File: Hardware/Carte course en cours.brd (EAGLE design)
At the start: 47 x 28.6 mm, 41 parts, among them J2 AVR_SPI_PROG_3X2NS, J3 PWR IN, J4 RC receiver, J5 ESC, J6 ESC, J7 MICRO-SD_CARD_SOCKET, J8 ESC, U1 V_REG_317SMD, U2 ATMEGA328P_TQFP, U3 FT232RL, U4 MPU6050, Y1 16MHz

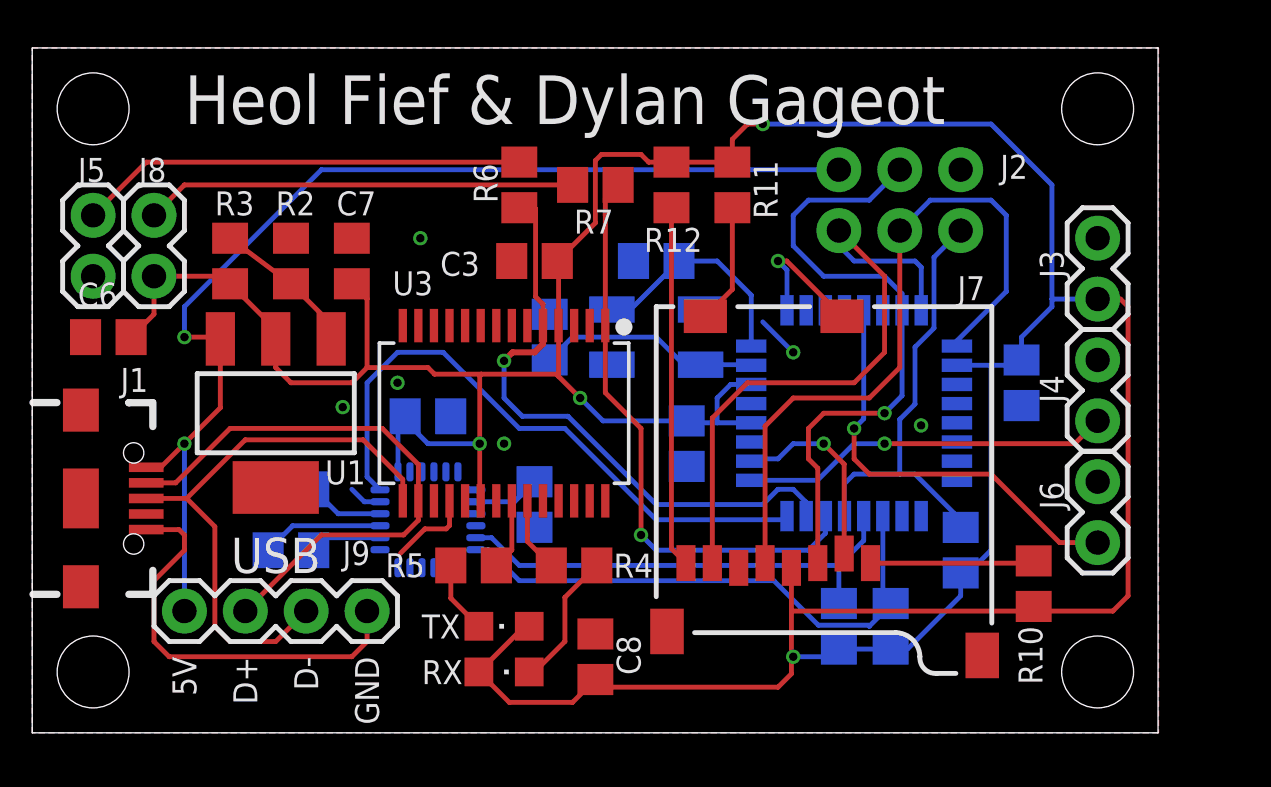
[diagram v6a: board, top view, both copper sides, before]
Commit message: Add heatsink plane
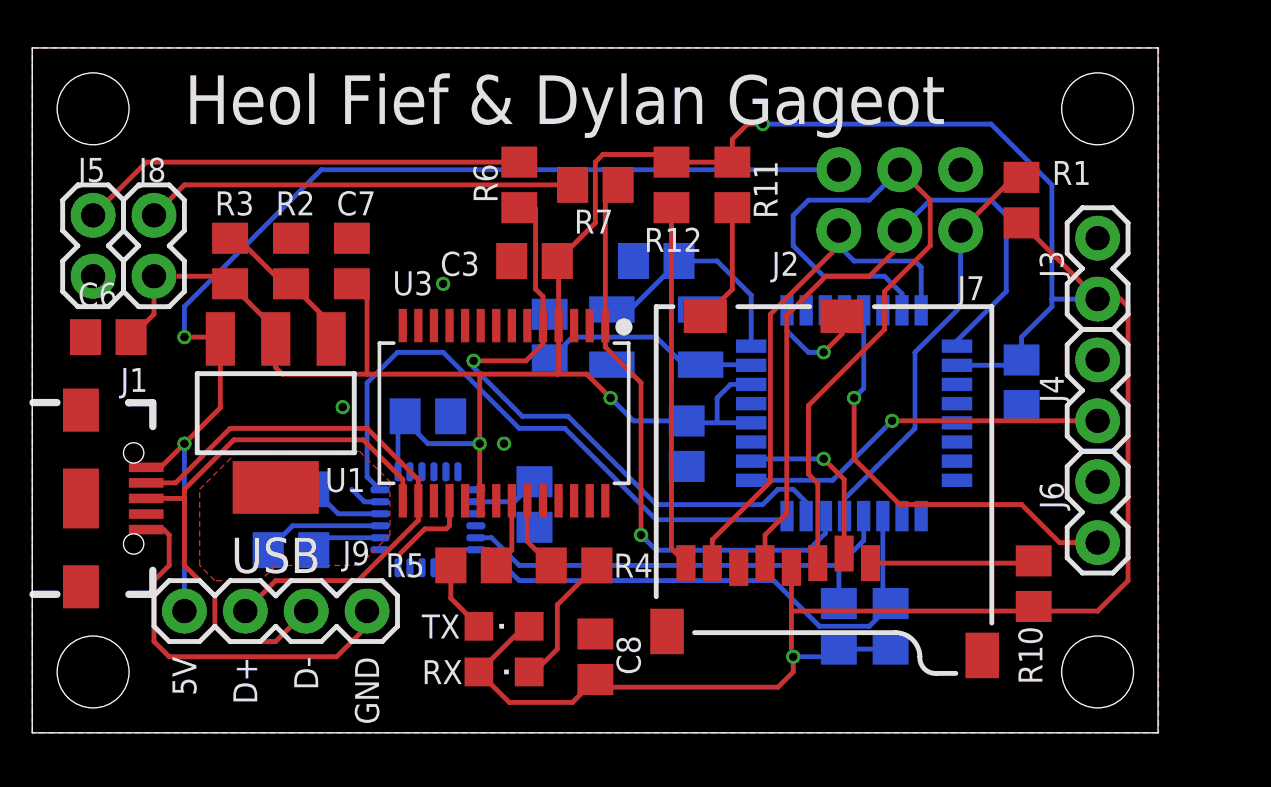
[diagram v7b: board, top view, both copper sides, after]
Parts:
- U1: value V_REG_317SMD -> LM317; device SparkFun-IC-Power:SOT223 -> bt_regulator:SOT-223-3
- moved R1 14.8 mm to (41.3, 22.2), flipped to the top
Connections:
- new net HEATSINK: U1.4
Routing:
- net +3V3: track 162.5 -> 152.0 mm
- net MOSI: track 26.4 -> 31.8 mm, vias 1 -> 0
- net MISO: track 26.5 -> 22.3 mm
- net GND: track 29.2 -> 26.1 mm, vias 6 -> 3
- net TX_AVR: track 25.4 -> 27.2 mm
- net RST: track 18.7 -> 17.4 mm
- net CARDDETECT: track 5.84 -> 4.58 mm
- net CS: track 8.26 -> 7.37 mm
- net SCK: track 29.6 -> 28.8 mm
- added copper zone on layer 1, net HEATSINK

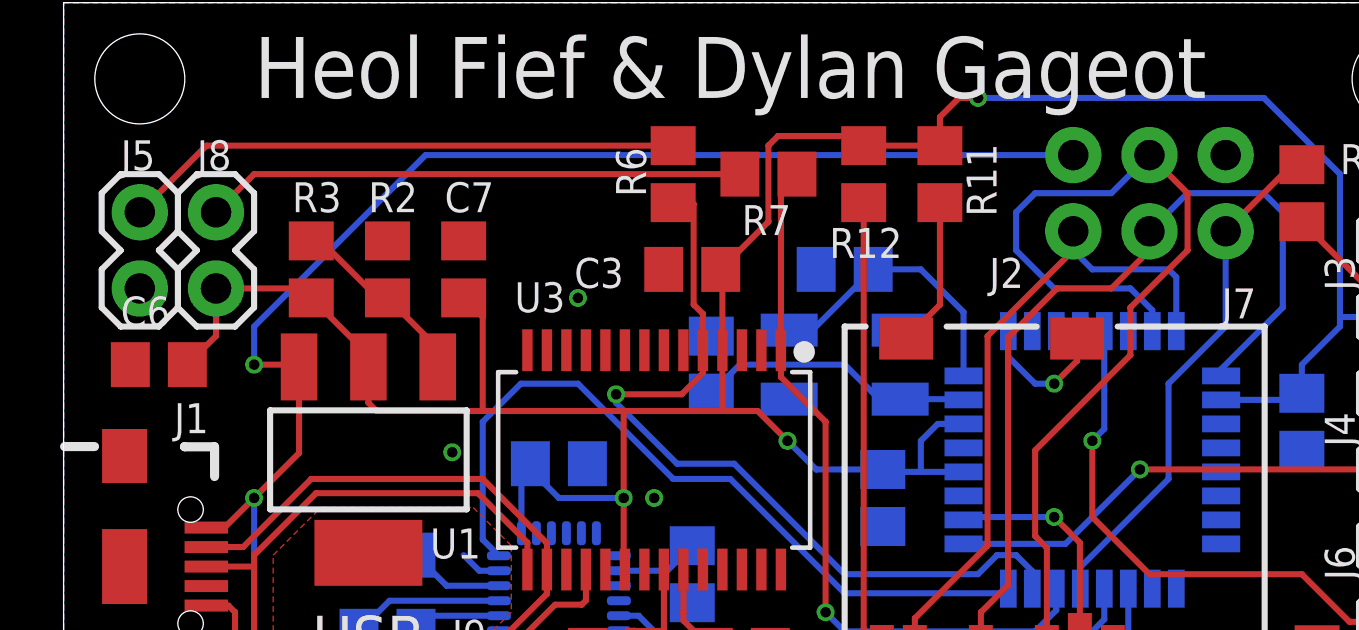
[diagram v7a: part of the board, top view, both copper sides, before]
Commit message: Improve trace shape
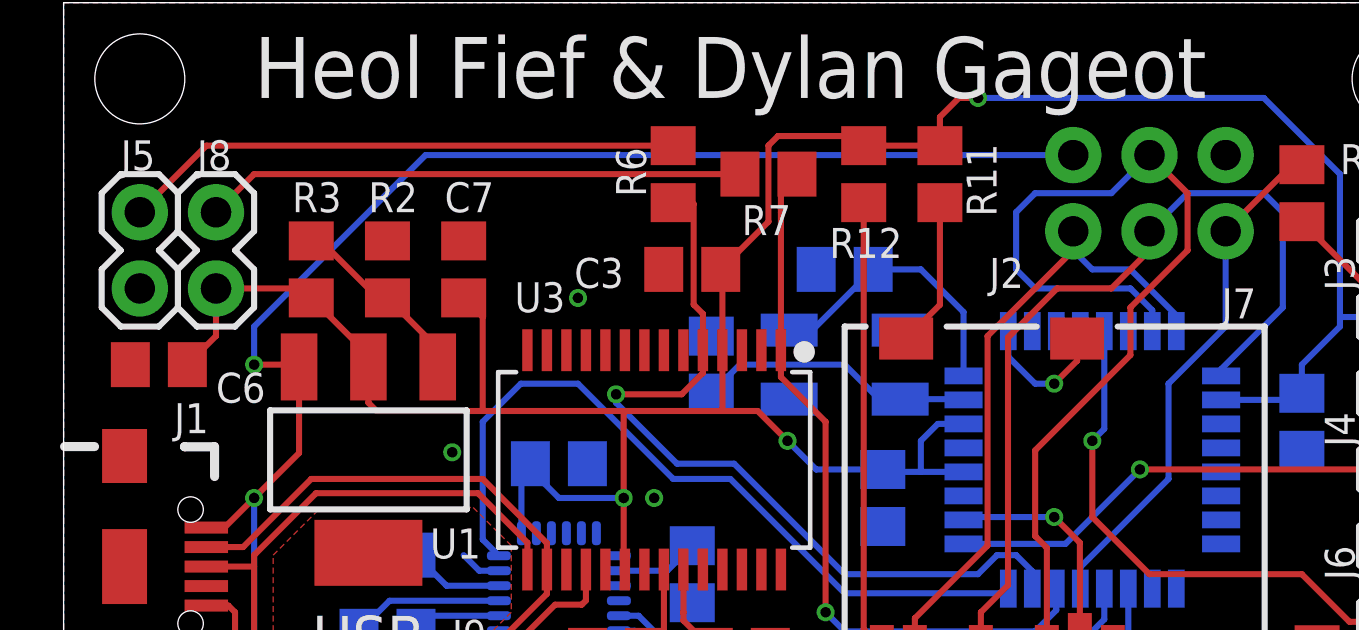
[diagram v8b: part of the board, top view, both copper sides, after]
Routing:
- net MISO: track 22.3 -> 21.6 mm
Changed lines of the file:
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@@
 <layer number="27" name="tValues" color="7" fill="1" visible="no" active="yes"/>
 <layer number="28" name="bValues" color="7" fill="1" visible="no" active="yes"/>
-<layer number="29" name="tStop" color="7" fill="3" visible="no" active="yes"/>
+<layer number="29" name="tStop" color="7" fill="1" visible="no" active="yes"/>
 <layer number="30" name="bStop" color="7" fill="6" visible="no" active="yes"/>
 <layer number="31" name="tCream" color="7" fill="4" visible="no" active="yes"/>
@@
 </element>
 <element name="C6" library="rcl" library_urn="urn:adsk.eagle:library:334" package="C0805" package3d_urn="urn:adsk.eagle:package:23617/2" value="4.7u" x="3.175" y="16.51" smashed="yes">
-<attribute name="NAME" x="1.905" y="17.78" size="1" layer="25"/>
+<attribute name="NAME" x="5.08" y="15.24" size="1" layer="25"/>
 <attribute name="VALUE" x="1.905" y="13.97" size="1" layer="27"/>
 </element>
@@
 <contactref element="J2" pad="1"/>
 <contactref element="J7" pad="DO"/>
-<wire x1="37.09" y1="17.6276" x2="37.09" y2="19.425" width="0.2032" layer="16"/>
-<wire x1="37.09" y1="19.425" x2="36.83" y2="19.685" width="0.2032" layer="16"/>
-<wire x1="36.83" y1="19.685" x2="34.29" y2="19.685" width="0.2032" layer="16"/>
+<wire x1="37.09" y1="17.6276" x2="37.09" y2="18.155" width="0.2032" layer="16"/>
+<wire x1="37.09" y1="18.155" x2="35.56" y2="19.685" width="0.2032" layer="16"/>
+<wire x1="35.56" y1="19.685" x2="34.29" y2="19.685" width="0.2032" layer="16"/>
 <wire x1="34.29" y1="19.685" x2="33.655" y2="20.32" width="0.2032" layer="16"/>
 <wire x1="33.655" y1="20.32" x2="33.655" y2="20.955" width="0.2032" layer="16"/>
@@
 <wire x1="34.925" y1="22.225" x2="32.385" y2="22.225" width="0.2032" layer="16"/>
 <wire x1="32.385" y1="22.225" x2="31.75" y2="21.59" width="0.2032" layer="16"/>
-<wire x1="31.75" y1="21.59" x2="31.75" y2="20.32" width="0.2032" layer="16"/>
-<wire x1="31.75" y1="20.32" x2="33.02" y2="19.05" width="0.2032" layer="16"/>
-<wire x1="33.02" y1="19.05" x2="35.56" y2="19.05" width="0.2032" layer="16"/>
+<wire x1="31.75" y1="21.59" x2="31.75" y2="19.685" width="0.2032" layer="16"/>
+<wire x1="31.75" y1="19.685" x2="32.385" y2="19.05" width="0.2032" layer="16"/>
+<wire x1="32.385" y1="19.05" x2="35.56" y2="19.05" width="0.2032" layer="16"/>
 <wire x1="35.56" y1="19.05" x2="36.29" y2="18.32" width="0.2032" layer="16"/>
 <wire x1="36.29" y1="17.6276" x2="36.29" y2="18.32" width="0.2032" layer="16"/>
